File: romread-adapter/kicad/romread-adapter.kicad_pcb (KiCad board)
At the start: 2 copper layers, 100 x 100 mm, 27 parts

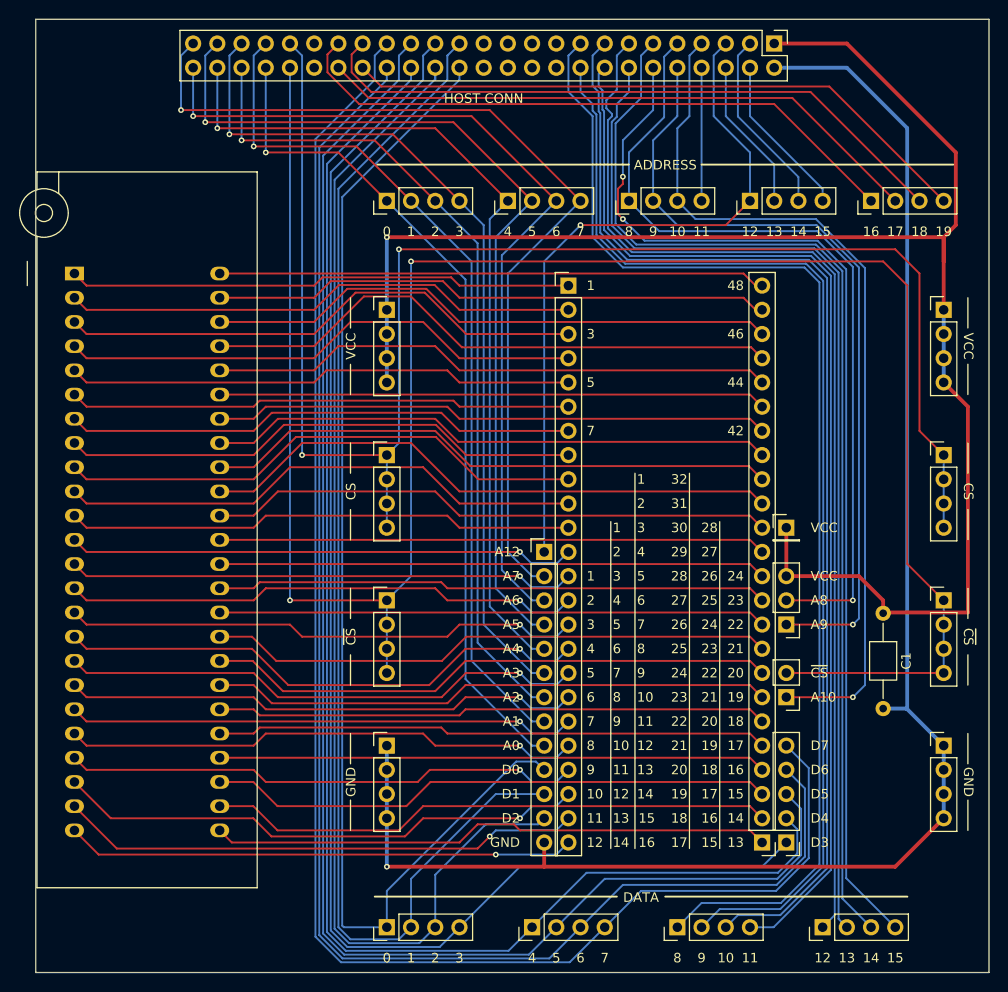
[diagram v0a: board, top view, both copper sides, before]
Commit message: romread-adapter sch pcb: Add C2
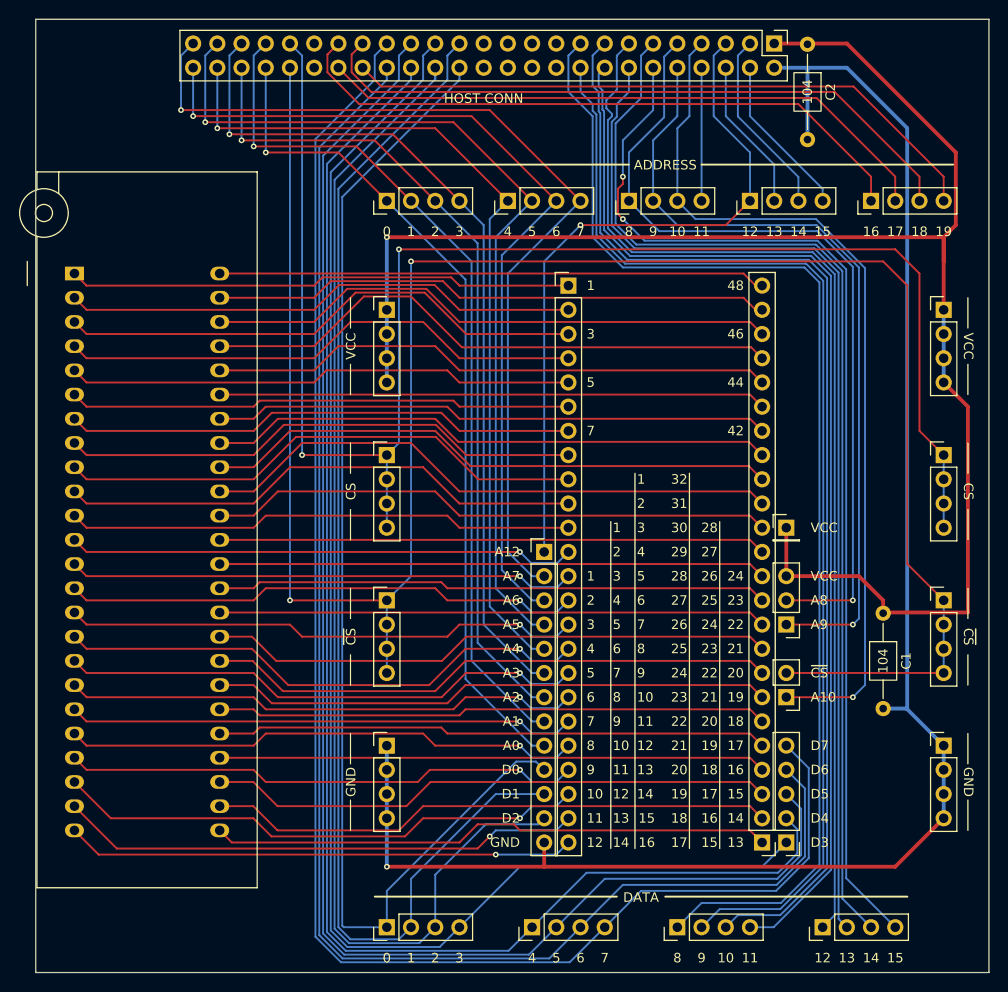
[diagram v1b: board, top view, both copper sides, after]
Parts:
- added C2: 104, Capacitor_THT:C_Axial_L3.8mm_D2.6mm_P10.00mm_Horizontal, F.Cu at (182.6, 53.4)
- C1: value 0.1 μF -> 104
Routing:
- net GND: track 168.9 -> 176.4 mm
- net A18: track 68.7 -> 70.1 mm
- net A17: track 64.2 -> 65.7 mm
- net A19: track 66.7 -> 68.2 mm
- net A16: track 66.1 -> 67.6 mm
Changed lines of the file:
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@@
 			)
 		)
-		(property "Value" "0.1 μF"
-			(at 5 2.42 90)
-			(layer "F.Fab")
+		(property "Value" "104"
+			(at 5 0 90)
+			(layer "F.SilkS")
 			(effects
 				(font
@@
 		)
 	)
+	(footprint "Capacitor_THT:C_Axial_L3.8mm_D2.6mm_P10.00mm_Horizontal"
+		(layer "F.Cu")
+		(at 182.5625 53.42 -90)
+		(descr "C, Axial series, Axial, Horizontal, pin pitch=10mm, length*diameter=3.8*2.6mm^2, http://www.vishay.com/docs/45231/arseries.pdf")
+		(tags "C Axial series Axial Horizontal pin pitch 10mm  length 3.8mm diameter 2.6mm")
+		(property "Reference" "C2"
+			(at 5 -2.42 90)
+			(layer "F.SilkS")
+			(effects
+				(font
+					(size 1 1)
+					(thickness 0.15)
+				)
+			)
+		)
+		(property "Value" "104"
+			(at 5 0 90)
+			(layer "F.SilkS")
+			(effects
+				(font
+					(size 1 1)
+					(thickness 0.15)
+				)
+			)
+		)
+		(property "Datasheet" "~"
+			(at 0 0 90)
+			(layer "F.Fab")
+			(hide yes)
+			(effects
+				(font
+					(size 1.27 1.27)
+					(thickness 0.15)
+				)
+			)
+		)
+		(property "Description" "Unpolarized capacitor"
+			(at 0 0 90)
+			(layer "F.Fab")
+			(hide yes)
+			(effects
+				(font
+					(size 1.27 1.27)
+					(thickness 0.15)
+				)
+			)
+		)
+		(property ki_fp_filters "C_*")
+		(sheetname "/")
+		(sheetfile "romread-adapter.kicad_sch")
+		(attr through_hole)
+		(fp_line
+			(start 1.04 0)
+			(end 2.98 0)
+			(stroke
+				(width 0.12)
+				(type solid)
+			)
+			(layer "F.SilkS")
+		)
+		(fp_line
+			(start 8.96 0)
+			(end 7.02 0)
+			(stroke
+				(width 0.12)
+				(type solid)
+			)
+			(layer "F.SilkS")
+		)
+		(fp_rect
+			(start 2.98 -1.42)
+			(end 7.02 1.42)
+			(stroke
+				(width 0.12)
+				(type solid)
+			)
+			(fill no)
+			(layer "F.SilkS")
+		)
+		(fp_rect
+			(start -1.05 -1.55)
+			(end 11.05 1.55)
+			(stroke
+				(width 0.05)
+				(type solid)
+			)
+			(fill no)
+			(layer "F.CrtYd")
+		)
+		(fp_line
+			(start 0 0)
+			(end 3.1 0)
+			(stroke
+				(width 0.1)
+				(type solid)
+			)
+			(layer "F.Fab")
+		)
+		(fp_line
+			(start 10 0)
+			(end 6.9 0)
+			(stroke
+				(width 0.1)
+				(type solid)
+			)
+			(layer "F.Fab")
+		)
+		(fp_rect
+			(start 3.1 -1.3)
+			(end 6.9 1.3)
+			(stroke
+				(width 0.1)
+				(type solid)
+			)
+			(fill no)
+			(layer "F.Fab")
+		)
+		(fp_text user "${REFERENCE}"
+			(at 5 0 90)
+			(layer "F.Fab")
+			(effects
+				(font
+					(size 0.76 0.76)
+					(thickness 0.114)
+				)
+			)
+		)
+		(pad "1" thru_hole circle
+			(at 0 0 270)
+			(size 1.6 1.6)
+			(drill 0.8)
+			(layers "*.Cu" "*.Mask")
+			(remove_unused_layers no)
+			(net 2 "VCC")
+			(pintype "passive")
+		)
+		(pad "2" thru_hole circle
+			(at 10 0 270)
+			(size 1.6 1.6)
+			(drill 0.8)
+			(layers "*.Cu" "*.Mask")
+			(remove_unused_layers no)
+			(net 1 "GND")
+			(pintype "passive")
+		)
+		(embedded_fonts no)
+		(model "${KICAD9_3DMODEL_DIR}/Capacitor_THT.3dshapes/C_Axial_L3.8mm_D2.6mm_P10.00mm_Horizontal.step"
+			(offset
+				(xyz 0 0 0)
+			)
+			(scale
+				(xyz 1 1 1)
+			)
+			(rotate
+				(xyz 0 0 0)
+			)
+		)
+	)
 	(gr_line
 		(start 137.16 142.840408)
@@
 	)
 	(segment
+		(start 182.5625 63.42)
+		(end 182.5625 55.88)
+		(width 0.4)
+		(layer "B.Cu")
+		(net 1)
+	)
+	(segment
 		(start 138.43 129.54)
 		(end 138.43 127)
@@
 	)
 	(segment
-		(start 186.69 55.88)
+		(start 182.5625 55.88)
 		(end 179.07 55.88)
 		(width 0.4)
@@
 	)
 	(segment
+		(start 186.69 55.88)
+		(end 182.5625 55.88)
+		(width 0.4)
+		(layer "B.Cu")
+		(net 1)
+	)
+	(segment
 		(start 138.43 134.62)
 		(end 138.43 132.08)
@@
 	)
 	(segment
-		(start 191.77 69.85)
-		(end 180.975 59.055)
+		(start 191.77 67.31)
+		(end 183.515 59.055)
 		(width 0.2)
 		(layer "F.Cu")
@@
 	)
 	(segment
-		(start 180.975 59.055)
+		(start 191.77 69.85)
+		(end 191.77 67.31)
+		(width 0.2)
+		(layer "F.Cu")
+		(net 10)
+	)
+	(segment
+		(start 183.515 59.055)
 		(end 136.525 59.055)
 		(width 0.2)
@@
 	)
 	(segment
-		(start 134.739 56.35676)
-		(end 134.739 54.491)
+		(start 134.739 54.491)
+		(end 135.89 53.34)
 		(width 0.2)
 		(layer "F.Cu")
@@
 	)
 	(segment
-		(start 134.739 54.491)
-		(end 135.89 53.34)
+		(start 136.80224 58.42)
+		(end 134.739 56.35676)
 		(width 0.2)
 		(layer "F.Cu")
@@
 	)
 	(segment
-		(start 136.80224 58.42)
-		(end 134.739 56.35676)
+		(start 194.31 67.31)
+		(end 185.42 58.42)
+		(width 0.2)
+		(layer "F.Cu")
+		(net 13)
+	)
+	(segment
+		(start 185.42 58.42)
+		(end 136.80224 58.42)
 		(width 0.2)
 		(layer "F.Cu")
@@
 	(segment
 		(start 194.31 69.85)
-		(end 182.88 58.42)
+		(end 194.31 67.31)
 		(width 0.2)
 		(layer "F.Cu")
@@
 	)
 	(segment
-		(start 182.88 58.42)
-		(end 136.80224 58.42)
+		(start 134.739 56.35676)
+		(end 134.739 54.491)
 		(width 0.2)
 		(layer "F.Cu")
@@
 	)
 	(segment
-		(start 137.862 57.852)
-		(end 184.852 57.852)
+		(start 187.392 57.852)
+		(end 196.85 67.31)
 		(width 0.2)
 		(layer "F.Cu")
@@
 	)
 	(segment
-		(start 135.89 55.88)
-		(end 137.862 57.852)
+		(start 196.85 67.31)
+		(end 196.85 69.85)
 		(width 0.2)
 		(layer "F.Cu")
@@
 	)
 	(segment
-		(start 184.852 57.852)
-		(end 196.85 69.85)
+		(start 137.862 57.852)
+		(end 187.392 57.852)
+		(width 0.2)
+		(layer "F.Cu")
+		(net 27)
+	)
+	(segment
+		(start 135.89 55.88)
+		(end 137.862 57.852)
 		(width 0.2)
 		(layer "F.Cu")
@@
 	)
 	(segment
-		(start 179.07 59.69)
-		(end 135.53224 59.69)
+		(start 189.23 69.85)
+		(end 189.23 67.31)
+		(width 0.2)
+		(layer "F.Cu")
+		(net 50)
+	)
+	(segment
+		(start 189.23 67.31)
+		(end 181.61 59.69)
 		(width 0.2)
 		(layer "F.Cu")
@@
 	)
 	(segment
-		(start 135.53224 59.69)
-		(end 132.199 56.35676)
+		(start 181.61 59.69)
+		(end 135.53224 59.69)
 		(width 0.2)
 		(layer "F.Cu")
@@
 	)
 	(segment
-		(start 189.23 69.85)
-		(end 179.07 59.69)
+		(start 135.53224 59.69)
+		(end 132.199 56.35676)
 		(width 0.2)
 		(layer "F.Cu")

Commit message: romread-adapter pcb: Add mounting holes
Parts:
- added REF**: MountingHole_3.2mm_M3, MountingHole:MountingHole_3.2mm_M3, F.Cu at (105.1, 54.3)
- added REF**: MountingHole_3.2mm_M3, MountingHole:MountingHole_3.2mm_M3, F.Cu at (198.1, 54.3)
- added REF**: MountingHole_3.2mm_M3, MountingHole:MountingHole_3.2mm_M3, F.Cu at (198.1, 147.3)
- added REF**: MountingHole_3.2mm_M3, MountingHole:MountingHole_3.2mm_M3, F.Cu at (105.1, 147.3)

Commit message: romread-adapter pcb: Improve text and fix mounthole warnings
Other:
- board text added: "revision ${REVISION} https://github.com/0cjs/hwdev"
- board text added: "romread-adapter"
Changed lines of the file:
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@@
+		)
+	)
+	(gr_text "revision ${REVISION}\nhttps://github.com/0cjs/hwdev"
+		(at 107.95 64.77 0)
+		(layer "F.SilkS")
+		(effects
+			(font
+				(size 1 1)
+				(thickness 0.1)
+			)
+			(justify left bottom)
 		)
 	)
@@
 		)
 	)
+	(gr_text "romread-adapter"
+		(at 107.684905 61.585935 0)
+		(layer "F.SilkS")
+		(effects
+			(font
+				(size 2 2)
+				(thickness 0.25)
+			)
+			(justify left bottom)
+		)
+	)
 	(gr_text "17"
 		(at 191.77 73.66 0)
@@
 		)
 	)
-	(gr_text_box "romread-adapter ${REVISION}\nhttps://github.com/0cjs/hwdev"
-		(start 105.370153 59.597897)
-		(end 133.389847 64.862103)
-		(margins 1.0025 1.0025 1.0025 1.0025)
-		(layer "F.SilkS")
-		(effects
-			(font
-				(size 1 1)
-				(thickness 0.1)
-			)
-			(justify left top)
-		)
-		(border no)
-		(stroke
-			(width 0)
-			(type solid)
-		)
-	)
